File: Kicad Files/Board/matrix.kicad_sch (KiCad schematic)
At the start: 145 parts

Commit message: PCB Space
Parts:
- removed D61, D62, D65, D66, D67, D68: D_Small, symbol mechanical_keyboard:D_Small
- removed MX15, MX47, MX49, MX50, MX51, MX53, MX54, MX55, MX59, MX60, MX61, MX64, MX65, MX66, MX67: MX_SW_solder, PCM_marbastlib-mx:SW_MX_1u, symbol mechanical_keyboard:MX_SW_solder
- removed S1, S2, S3, S4, S5: MX_stab, PCM_marbastlib-mx:STAB_MX_P_6.25u, symbol mechanical_keyboard:MX_stab
- added D1, D74: D_Small, mechanical_keyboard:D_0402_1005Metric, symbol mechanical_keyboard:D_Small
- added MX25: O, mechanical_keyboard:SW_MX_1u, symbol mechanical_keyboard:MX_SW_solder
- added MX26: P, mechanical_keyboard:SW_MX_1u, symbol mechanical_keyboard:MX_SW_solder
- added MX27: [, mechanical_keyboard:SW_MX_1u, symbol mechanical_keyboard:MX_SW_solder
- added MX28: ], mechanical_keyboard:SW_MX_1u, symbol mechanical_keyboard:MX_SW_solder
- added MX29: Enter, mechanical_keyboard:SW_MX_1u, symbol mechanical_keyboard:MX_SW_solder
- added MX30: Insert, mechanical_keyboard:SW_MX_1u, symbol mechanical_keyboard:MX_SW_solder
- added MX42: ', mechanical_keyboard:SW_MX_1u, symbol mechanical_keyboard:MX_SW_solder
- added MX43: \, mechanical_keyboard:SW_MX_1u, symbol mechanical_keyboard:MX_SW_solder
- added MX44: Delete, mechanical_keyboard:SW_MX_1u, symbol mechanical_keyboard:MX_SW_solder
- added MX45: Mode, mechanical_keyboard:SW_MX_1u, symbol mechanical_keyboard:MX_SW_solder
- added MX62: Space, mechanical_keyboard:SW_MX_1u, symbol mechanical_keyboard:MX_SW_solder
- D10, D11, D12, D13, D14, D15, D16, D17, D18, D19, D2, D20, D21, D22, D23, D24, D25, D26, D27, D28, D29, D3, D30, D31, D32, D33, D34, D35, D36, D37, D38, D39, D4, D40, D41, D42, D43, D44, D45, D46, D47, D48, D49, D5, D50, D51, D52, D53, D54, D55, D56, D57, D58, D59, D6, D60, D63, D64, D69, D7, D70, D71, D8, D9: footprint (none) -> mechanical_keyboard:D_0402_1005Metric
- MX1: value MX_SW_solder -> ESC; footprint PCM_marbastlib-mx:SW_MX_1u -> mechanical_keyboard:SW_MX_1u
- MX10: value MX_SW_solder -> 8; footprint PCM_marbastlib-mx:SW_MX_1u -> mechanical_keyboard:SW_MX_1u
- MX11: value MX_SW_solder -> 9; footprint PCM_marbastlib-mx:SW_MX_1u -> mechanical_keyboard:SW_MX_1u
- MX12: value MX_SW_solder -> 0; footprint PCM_marbastlib-mx:SW_MX_1u -> mechanical_keyboard:SW_MX_1u
- MX13: value MX_SW_solder -> -; footprint PCM_marbastlib-mx:SW_MX_1u -> mechanical_keyboard:SW_MX_1u
- MX14: value MX_SW_solder -> +; footprint PCM_marbastlib-mx:SW_MX_1u -> mechanical_keyboard:SW_MX_1u
- MX15: renamed from MX52; value MX_SW_solder -> BackSpace; footprint PCM_marbastlib-mx:SW_MX_1u -> mechanical_keyboard:SW_MX_1u
- MX16: value MX_SW_solder -> Tab; footprint PCM_marbastlib-mx:SW_MX_1u -> mechanical_keyboard:SW_MX_1u
- MX17: value MX_SW_solder -> Q; footprint PCM_marbastlib-mx:SW_MX_1u -> mechanical_keyboard:SW_MX_1u
- MX18: value MX_SW_solder -> W; footprint PCM_marbastlib-mx:SW_MX_1u -> mechanical_keyboard:SW_MX_1u
- MX19: value MX_SW_solder -> E; footprint PCM_marbastlib-mx:SW_MX_1u -> mechanical_keyboard:SW_MX_1u
- MX2: value MX_SW_solder -> `; footprint PCM_marbastlib-mx:SW_MX_1u -> mechanical_keyboard:SW_MX_1u
- MX20: value MX_SW_solder -> R; footprint PCM_marbastlib-mx:SW_MX_1u -> mechanical_keyboard:SW_MX_1u
- MX21: value MX_SW_solder -> T; footprint PCM_marbastlib-mx:SW_MX_1u -> mechanical_keyboard:SW_MX_1u
- MX22: value MX_SW_solder -> Y; footprint PCM_marbastlib-mx:SW_MX_1u -> mechanical_keyboard:SW_MX_1u
- MX23: value MX_SW_solder -> U; footprint PCM_marbastlib-mx:SW_MX_1u -> mechanical_keyboard:SW_MX_1u
- MX24: value MX_SW_solder -> I; footprint PCM_marbastlib-mx:SW_MX_1u -> mechanical_keyboard:SW_MX_1u
- MX3: value MX_SW_solder -> 1; footprint PCM_marbastlib-mx:SW_MX_1u -> mechanical_keyboard:SW_MX_1u
- MX31: renamed from MX25; value MX_SW_solder -> CapsLock; footprint PCM_marbastlib-mx:SW_MX_1u -> mechanical_keyboard:SW_MX_1u
- MX32: renamed from MX27; value MX_SW_solder -> A; footprint PCM_marbastlib-mx:SW_MX_1u -> mechanical_keyboard:SW_MX_1u
- MX33: renamed from MX29; value MX_SW_solder -> S; footprint PCM_marbastlib-mx:SW_MX_1u -> mechanical_keyboard:SW_MX_1u
- MX34: renamed from MX31; value MX_SW_solder -> D; footprint PCM_marbastlib-mx:SW_MX_1u -> mechanical_keyboard:SW_MX_1u
- MX35: renamed from MX33; value MX_SW_solder -> F; footprint PCM_marbastlib-mx:SW_MX_1u -> mechanical_keyboard:SW_MX_1u
- MX36: renamed from MX35; value MX_SW_solder -> G; footprint PCM_marbastlib-mx:SW_MX_1u -> mechanical_keyboard:SW_MX_1u
- MX37: value MX_SW_solder -> H; footprint PCM_marbastlib-mx:SW_MX_1u -> mechanical_keyboard:SW_MX_1u
- MX38: renamed from MX39; value MX_SW_solder -> J; footprint PCM_marbastlib-mx:SW_MX_1u -> mechanical_keyboard:SW_MX_1u
- MX39: renamed from MX41; value MX_SW_solder -> K; footprint PCM_marbastlib-mx:SW_MX_1u -> mechanical_keyboard:SW_MX_1u
- MX4: value MX_SW_solder -> 2; footprint PCM_marbastlib-mx:SW_MX_1u -> mechanical_keyboard:SW_MX_1u
- MX40: renamed from MX43; value MX_SW_solder -> L; footprint PCM_marbastlib-mx:SW_MX_1u -> mechanical_keyboard:SW_MX_1u
- MX41: renamed from MX45; value MX_SW_solder -> ;; footprint PCM_marbastlib-mx:SW_MX_1u -> mechanical_keyboard:SW_MX_1u
- MX46: renamed from MX26; value MX_SW_solder -> LShift; footprint PCM_marbastlib-mx:SW_MX_1u -> mechanical_keyboard:SW_MX_1u
- MX47: renamed from MX28; value MX_SW_solder -> Z; footprint PCM_marbastlib-mx:SW_MX_1u -> mechanical_keyboard:SW_MX_1u
- MX48: renamed from MX30; value MX_SW_solder -> X; footprint PCM_marbastlib-mx:SW_MX_1u -> mechanical_keyboard:SW_MX_1u
- MX49: renamed from MX32; value MX_SW_solder -> C; footprint PCM_marbastlib-mx:SW_MX_1u -> mechanical_keyboard:SW_MX_1u
- MX5: value MX_SW_solder -> 3; footprint PCM_marbastlib-mx:SW_MX_1u -> mechanical_keyboard:SW_MX_1u
- MX50: renamed from MX34; value MX_SW_solder -> V; footprint PCM_marbastlib-mx:SW_MX_1u -> mechanical_keyboard:SW_MX_1u
- MX51: renamed from MX36; value MX_SW_solder -> B; footprint PCM_marbastlib-mx:SW_MX_1u -> mechanical_keyboard:SW_MX_1u
- MX52: renamed from MX38; value MX_SW_solder -> N; footprint PCM_marbastlib-mx:SW_MX_1u -> mechanical_keyboard:SW_MX_1u
- MX53: renamed from MX40; value MX_SW_solder -> M; footprint PCM_marbastlib-mx:SW_MX_1u -> mechanical_keyboard:SW_MX_1u
- MX54: renamed from MX42; value MX_SW_solder -> ,; footprint PCM_marbastlib-mx:SW_MX_1u -> mechanical_keyboard:SW_MX_1u
- MX55: renamed from MX44; value MX_SW_solder -> .; footprint PCM_marbastlib-mx:SW_MX_1u -> mechanical_keyboard:SW_MX_1u
- MX56: renamed from MX46; value MX_SW_solder -> /; footprint PCM_marbastlib-mx:SW_MX_1u -> mechanical_keyboard:SW_MX_1u
- MX57: renamed from MX48; value MX_SW_solder -> RShift; footprint PCM_marbastlib-mx:SW_MX_1u -> mechanical_keyboard:SW_MX_1u
- MX58: renamed from MX70; value MX_SW_solder -> Up; footprint PCM_marbastlib-mx:SW_MX_1u -> mechanical_keyboard:SW_MX_1u
- MX59: renamed from MX56; value MX_SW_solder -> LCtrl; footprint PCM_marbastlib-mx:SW_MX_1u -> mechanical_keyboard:SW_MX_1u
- MX6: value MX_SW_solder -> 4; footprint PCM_marbastlib-mx:SW_MX_1u -> mechanical_keyboard:SW_MX_1u
- MX60: renamed from MX57; value MX_SW_solder -> Windows; footprint PCM_marbastlib-mx:SW_MX_1u -> mechanical_keyboard:SW_MX_1u
- MX61: renamed from MX58; value MX_SW_solder -> LAlt; footprint PCM_marbastlib-mx:SW_MX_1u -> mechanical_keyboard:SW_MX_1u
- MX63: value MX_SW_solder -> FN; footprint PCM_marbastlib-mx:SW_MX_1u -> mechanical_keyboard:SW_MX_1u
- MX64: renamed from MX62; value MX_SW_solder -> Left; footprint PCM_marbastlib-mx:SW_MX_1u -> mechanical_keyboard:SW_MX_1u
- MX65: renamed from MX68; value MX_SW_solder -> Down; footprint PCM_marbastlib-mx:SW_MX_1u -> mechanical_keyboard:SW_MX_1u
- MX66: renamed from MX69; value MX_SW_solder -> Right; footprint PCM_marbastlib-mx:SW_MX_1u -> mechanical_keyboard:SW_MX_1u
- MX7: value MX_SW_solder -> 5; footprint PCM_marbastlib-mx:SW_MX_1u -> mechanical_keyboard:SW_MX_1u
- MX8: value MX_SW_solder -> 6; footprint PCM_marbastlib-mx:SW_MX_1u -> mechanical_keyboard:SW_MX_1u
- MX9: value MX_SW_solder -> 7; footprint PCM_marbastlib-mx:SW_MX_1u -> mechanical_keyboard:SW_MX_1u
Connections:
- net COL14 is gone; now on net COL12: MX58.1, MX65.1
- net COL15 is gone; now on net COL13: MX66.1
- net COL0: now also MX1.1, MX16.1, MX31.1, MX46.1, MX59.1
- net COL1: now also MX17.1, MX2.1, MX32.1, MX47.1, MX60.1; no longer MX1.1, MX13.1, MX31.1, MX46.1, MX59.1
- net COL10: now also MX11.1, MX41.1, MX56.1, MX26.1; no longer MX10.1, MX22.1, MX40.1, MX55.1
- net COL11: now also MX12.1, MX57.1, MX64.1, MX27.1, MX42.1; no longer MX11.1, MX23.1, MX41.1, MX56.1
- net COL12: now also MX13.1, MX28.1, MX43.1; no longer MX12.1, MX24.1, MX57.1
- net COL13: now also MX14.1, MX29.1, MX30.1, MX44.1, MX45.1; no longer MX64.1
- net COL2: now also MX18.1, MX3.1, MX33.1, MX48.1, MX61.1; no longer MX14.1, MX2.1, MX32.1, MX47.1, MX60.1
- net COL3: now also MX19.1, MX34.1, MX4.1, MX49.1, MX62.1; no longer MX3.1, MX33.1, MX48.1, MX61.1
- net COL4: now also MX20.1, MX35.1, MX5.1, MX50.1; no longer MX16.1, MX34.1, MX4.1, MX49.1
- net COL5: now also MX21.1, MX36.1, MX51.1, MX6.1; no longer MX17.1, MX35.1, MX5.1, MX50.1
- net COL6: now also MX22.1, MX37.1, MX52.1, MX7.1; no longer MX18.1, MX36.1, MX51.1, MX6.1
- net COL7: now also MX23.1, MX38.1, MX53.1, MX63.1, MX8.1; no longer MX19.1, MX37.1, MX52.1, MX7.1
- net COL8: now also MX24.1, MX39.1, MX54.1, MX9.1; no longer MX20.1, MX38.1, MX53.1, MX63.1, MX8.1
- net COL9: now also MX10.1, MX40.1, MX55.1, MX25.1; no longer MX21.1, MX39.1, MX54.1, MX9.1
- net ROW0: now also D1.1 (K), D74.1 (K); no longer D48.1 (K), D54.1 (K), D55.1 (K)
- net ROW1: now also D48.1 (K), D55.1 (K); no longer D60.1 (K)
- net ROW2: now also D52.1 (K), D56.1 (K), D60.1 (K)
- net ROW3: no longer D52.1 (K)
- net ROW4: now also D54.1 (K); no longer D56.1 (K)
- net at D17.2 (A): now also MX19.2; no longer MX16.2
- net at D25.2 (A): now also MX27.2; no longer MX24.2
- net at D16.2 (A): now also MX18.2
- net at D18.2 (A): now also MX20.2; no longer MX17.2
- net at MX14.2: now also D74.2 (A); no longer D15.2 (A)
- net at D51.2 (A): now also MX42.2
- net at MX23.2: now also D21.2 (A); no longer D24.2 (A)
- net at D50.2 (A): now also MX29.2
- net at D20.2 (A): now also MX22.2; no longer MX19.2
- net at D54.2 (A): now also MX62.2
- net at D60.2 (A): now also MX45.2
- net at D23.2 (A): now also MX25.2; no longer MX22.2
- net at MX21.2: now also D19.2 (A); no longer D22.2 (A)
- net at D56.2 (A): now also MX44.2
- net at D55.2 (A): now also MX30.2
- net at D14.2 (A): now also MX16.2; no longer MX13.2
- net at D52.2 (A): now also MX43.2
- net EC1_SW1: no longer names the net of D48.2 (A)
- net EC1_SW1: now also MX28.2
- new net: D24.2 (A), MX26.2
- new net: D22.2 (A), MX24.2
- new net: D1.2 (A), MX13.2
- new net: D15.2 (A), MX17.2
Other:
- moved on the sheet: D10, D11, D12, D13, D14, D15, D16, D17, D18, D19, D2, D20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

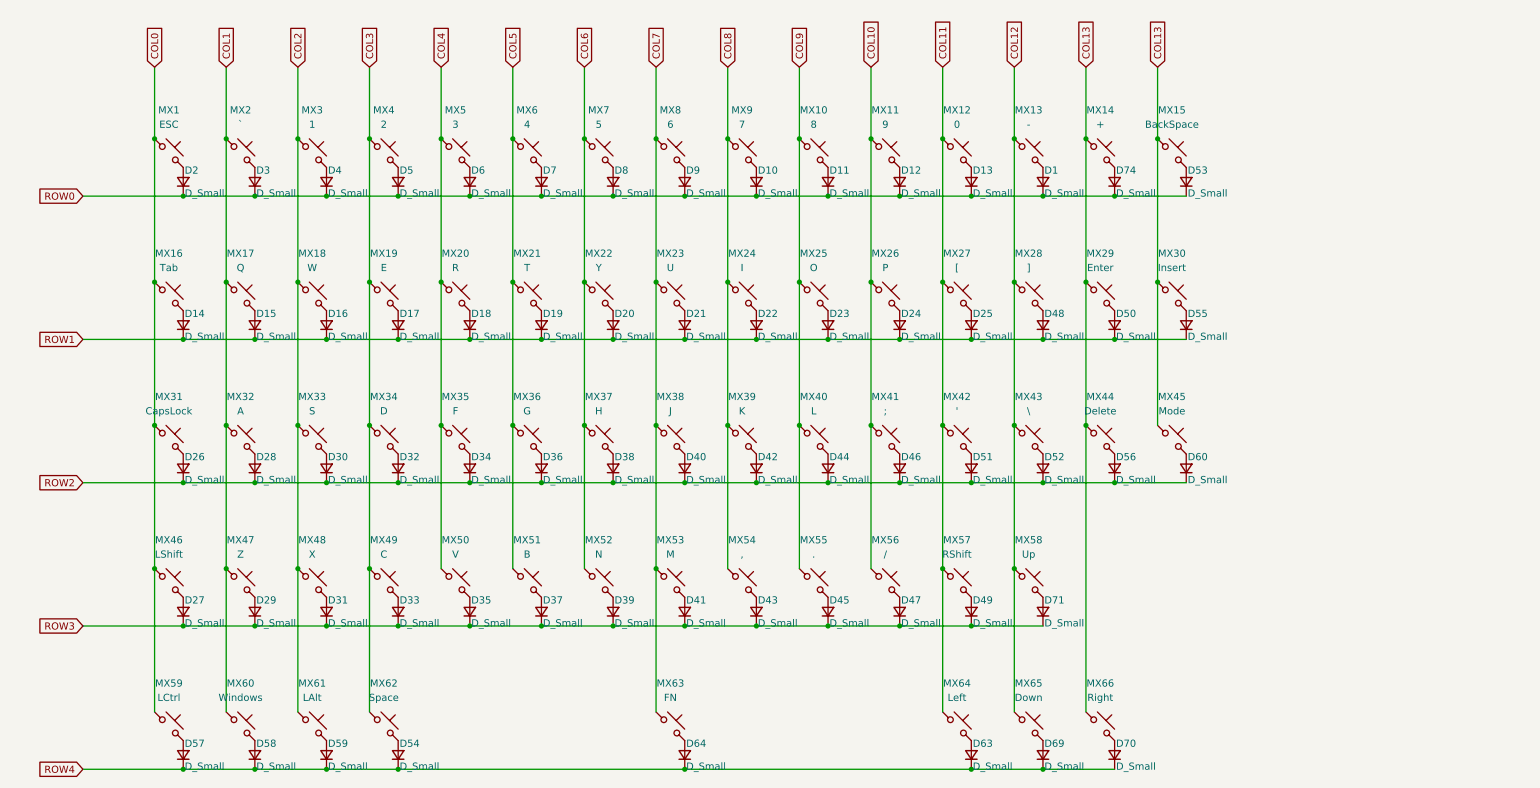
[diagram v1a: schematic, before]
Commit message: Matrix and Diode Done
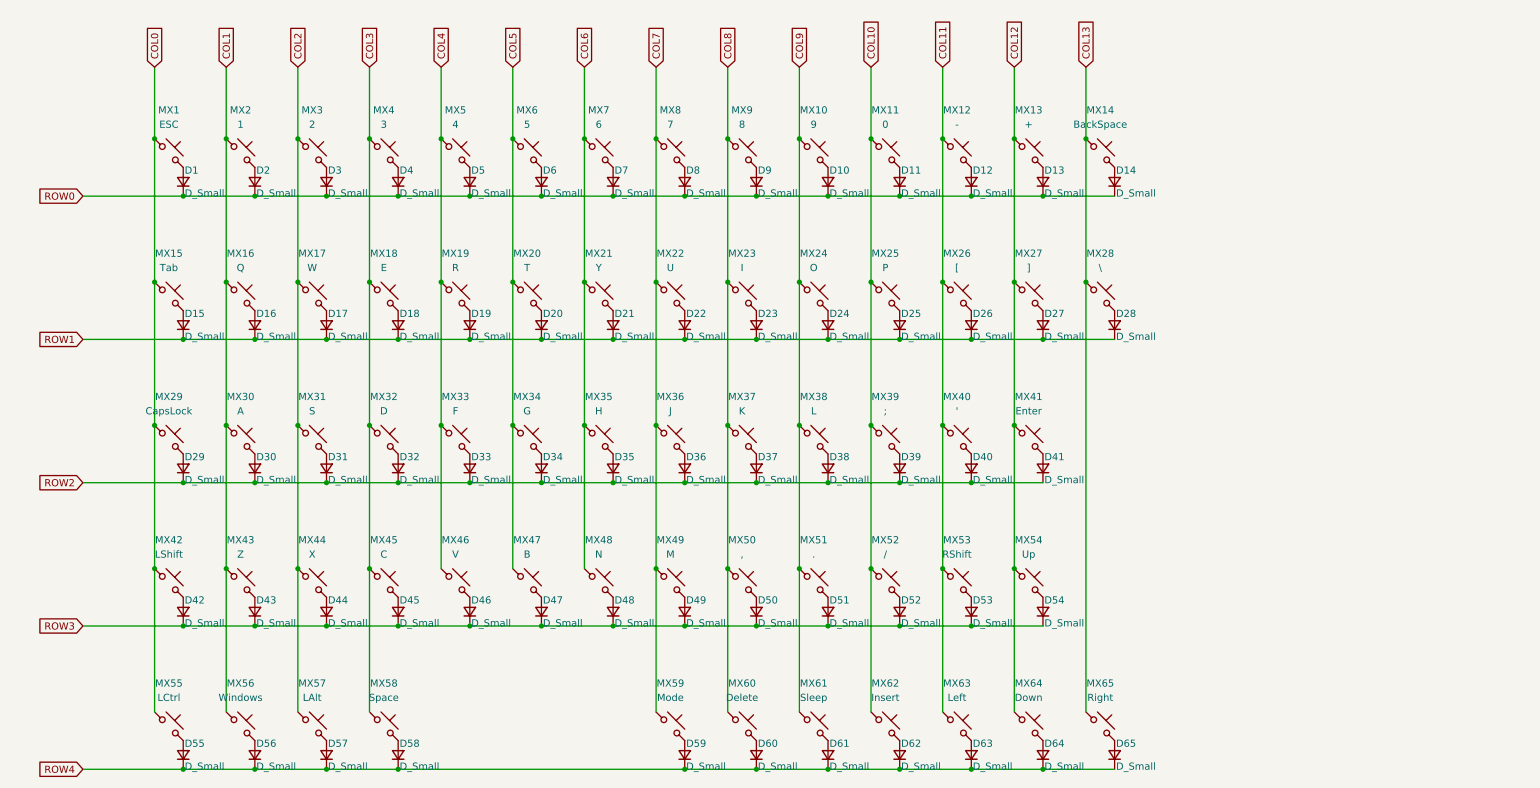
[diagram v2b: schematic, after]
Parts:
- removed D1, D55, D56, D71, D74: D_Small, mechanical_keyboard:D_0402_1005Metric, symbol mechanical_keyboard:D_Small
- removed MX55: ., mechanical_keyboard:SW_MX_1u, symbol mechanical_keyboard:MX_SW_solder
- removed MX56: /, mechanical_keyboard:SW_MX_1u, symbol mechanical_keyboard:MX_SW_solder
- removed MX57: RShift, mechanical_keyboard:SW_MX_1u, symbol mechanical_keyboard:MX_SW_solder
- removed MX58: Up, mechanical_keyboard:SW_MX_1u, symbol mechanical_keyboard:MX_SW_solder
- added D2, D54, D61, D62: D_Small, mechanical_keyboard:D_0402_1005Metric, symbol mechanical_keyboard:D_Small
- added MX60: Delete, mechanical_keyboard:SW_MX_1u, symbol mechanical_keyboard:MX_SW_solder
- added MX61: Sleep, mechanical_keyboard:SW_MX_1u, symbol mechanical_keyboard:MX_SW_solder
- added MX62: Insert, mechanical_keyboard:SW_MX_1u, symbol mechanical_keyboard:MX_SW_solder
- MX10: value 8 -> 9
- MX11: value 9 -> 0
- MX12: value 0 -> -
- MX13: value - -> +
- MX14: value + -> BackSpace
- MX15: value BackSpace -> Tab
- MX16: value Tab -> Q
- MX17: value Q -> W
- MX18: value W -> E
- MX19: value E -> R
- MX2: value ` -> 1
- MX20: value R -> T
- MX21: value T -> Y
- MX22: value Y -> U
- MX23: value U -> I
- MX24: value I -> O
- MX25: value O -> P
- MX26: value P -> [
- MX27: value [ -> ]
- MX28: value ] -> \
- MX29: value Enter -> CapsLock
- MX3: value 1 -> 2
- MX30: value Insert -> A
- MX31: value CapsLock -> S
- MX32: value A -> D
- MX33: value S -> F
- MX34: value D -> G
- MX35: value F -> H
- MX36: value G -> J
- MX37: value H -> K
- MX38: value J -> L
- MX39: value K -> ;
- MX4: value 2 -> 3
- MX40: value L -> '
- MX41: value ; -> Enter
- MX42: value ' -> LShift
- MX43: value \ -> Z
- MX44: value Delete -> X
- MX45: value Mode -> C
- MX46: value LShift -> V
- MX47: value Z -> B
- MX48: value X -> N
- MX49: value C -> M
- MX5: value 3 -> 4
- MX50: value V -> ,
- MX51: value B -> .
- MX52: value N -> /
- MX53: value M -> RShift
- MX54: value , -> Up
- MX59: renamed from MX63; value FN -> Mode
- MX6: value 4 -> 5
- MX7: value 5 -> 6
- MX8: value 6 -> 7
- MX9: value 7 -> 8
- renumbered D2 to D1, D57 to D55, D58 to D56, D59 to D57, D54 to D58, D64 to D59, D69 to D64, D70 to D65, MX59 to MX55, MX60 to MX56, MX61 to MX57, MX62 to MX58, MX64 to MX63, MX65 to MX64, MX66 to MX65
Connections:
- net COL0: now also MX15.1, MX29.1, MX42.1; no longer MX16.1, MX31.1, MX46.1
- net COL1: now also MX16.1, MX30.1, MX43.1; no longer MX17.1, MX32.1, MX47.1
- net COL10: now also MX25.1, MX39.1, MX52.1, MX62.1; no longer MX26.1, MX41.1
- net COL11: now also MX26.1, MX40.1, MX53.1; no longer MX27.1, MX42.1
- net COL12: now also MX27.1, MX41.1, MX54.1; no longer MX28.1, MX43.1
- net COL13: now also MX28.1; no longer MX15.1, MX29.1, MX30.1, MX44.1, MX45.1
- net COL2: now also MX17.1, MX31.1, MX44.1; no longer MX18.1, MX33.1, MX48.1
- net COL3: now also MX18.1, MX32.1, MX45.1; no longer MX19.1, MX34.1, MX49.1
- net COL4: now also MX19.1, MX33.1, MX46.1; no longer MX20.1, MX35.1, MX50.1
- net COL5: now also MX20.1, MX34.1, MX47.1; no longer MX21.1, MX36.1, MX51.1
- net COL6: now also MX21.1, MX35.1, MX48.1; no longer MX22.1, MX37.1, MX52.1
- net COL7: now also MX22.1, MX36.1, MX49.1; no longer MX23.1, MX38.1, MX53.1
- net COL8: now also MX23.1, MX37.1, MX50.1, MX60.1; no longer MX24.1, MX39.1, MX54.1
- net COL9: now also MX24.1, MX38.1, MX51.1, MX61.1; no longer MX25.1, MX40.1
- net ROW0: now also D14.1 (K), D2.1 (K); no longer D53.1 (K)
- net ROW1: now also D26.1 (K), D27.1 (K), D28.1 (K); no longer D14.1 (K), D48.1 (K), D50.1 (K)
- net ROW2: now also D29.1 (K), D31.1 (K), D33.1 (K), D35.1 (K), D37.1 (K), D39.1 (K), D41.1 (K); no longer D26.1 (K), D28.1 (K), D42.1 (K), D44.1 (K), D46.1 (K), D51.1 (K), D52.1 (K), D60.1 (K)
- net ROW3: now also D42.1 (K), D44.1 (K), D46.1 (K), D48.1 (K), D50.1 (K), D51.1 (K), D52.1 (K), D53.1 (K), D54.1 (K); no longer D27.1 (K), D29.1 (K), D31.1 (K), D33.1 (K), D35.1 (K), D37.1 (K), D39.1 (K), D41.1 (K)
- net ROW4: now also D60.1 (K), D61.1 (K), D62.1 (K)
- net at MX45.2: now also D45.2 (A); no longer D60.2 (A)
- net at MX40.2: now also D40.2 (A); no longer D44.2 (A)
- net at MX39.2: now also D39.2 (A); no longer D42.2 (A)
- net at D51.2 (A): now also MX51.2; no longer MX42.2
- net at MX21.2: now also D21.2 (A); no longer D19.2 (A)
- net at D17.2 (A): now also MX17.2; no longer MX19.2
- net at D11.2 (A): now also MX11.2; no longer MX10.2
- net at MX15.2: now also D15.2 (A); no longer D53.2 (A)
- net at MX14.2: now also D14.2 (A)
- net at D28.2 (A): now also MX28.2; no longer MX32.2
- net at MX48.2: now also D48.2 (A); no longer D31.2 (A)
- net at MX5.2: now also D5.2 (A); no longer D6.2 (A)
- net at MX22.2: now also D22.2 (A); no longer D20.2 (A)
- net at D25.2 (A): now also MX25.2; no longer MX27.2
- net at MX46.2: now also D46.2 (A); no longer D27.2 (A)
- net at D35.2 (A): now also MX35.2; no longer MX50.2
- net at MX18.2: now also D18.2 (A); no longer D16.2 (A)
- net at D7.2 (A): now also MX7.2; no longer MX6.2
- net at D29.2 (A): now also MX29.2; no longer MX47.2
- net at MX20.2: now also D20.2 (A); no longer D18.2 (A)
- net at MX23.2: now also D23.2 (A); no longer D21.2 (A)
- net at D4.2 (A): now also MX4.2; no longer MX3.2
- net at D12.2 (A): now also MX12.2; no longer MX11.2
- net at D38.2 (A): now also MX38.2; no longer MX37.2
- net at MX31.2: now also D31.2 (A); no longer D26.2 (A)
- net at D37.2 (A): now also MX37.2; no longer MX51.2
- net at MX26.2: now also D26.2 (A); no longer D24.2 (A)
- net at MX34.2: now also D34.2 (A); no longer D32.2 (A)
- net at MX24.2: now also D24.2 (A); no longer D22.2 (A)
- net at MX44.2: now also D44.2 (A)
- net at MX9.2: now also D9.2 (A); no longer D10.2 (A)
- net at MX41.2: now also D41.2 (A); no longer D46.2 (A)
- net at MX49.2: now also D49.2 (A); no longer D33.2 (A)
- net at MX2.2: now also D2.2 (A); no longer D3.2 (A)
- net at MX52.2: now also D52.2 (A); no longer D39.2 (A)
- net at D8.2 (A): now also MX8.2; no longer MX7.2
- net at D13.2 (A): now also MX13.2; no longer MX12.2
- net at MX54.2: now also D54.2 (A); no longer D43.2 (A)
- net at MX43.2: now also D43.2 (A); no longer D52.2 (A)
- net at D50.2 (A): now also MX50.2; no longer MX29.2
- net at MX16.2: now also D16.2 (A); no longer D14.2 (A)
- net at MX30.2: now also D30.2 (A)
- net at MX33.2: now also D33.2 (A); no longer D30.2 (A)
- net at MX53.2: now also D53.2 (A); no longer D41.2 (A)
- net at D47.2 (A): now also MX47.2
- new net: D61.2 (A), MX61.2
- new net: D32.2 (A), MX32.2
- new net: D6.2 (A), MX6.2
- new net: D62.2 (A), MX62.2
- new net: D27.2 (A), MX27.2
- new net: D60.2 (A), MX60.2
- new net: D3.2 (A), MX3.2
- new net: D10.2 (A), MX10.2
- new net: D42.2 (A), MX42.2
- new net: D19.2 (A), MX19.2

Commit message: Switch Update
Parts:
- added D66: D_Small, mechanical_keyboard:D_0402_1005Metric, symbol mechanical_keyboard:D_Small
- added MX66: Delete, mechanical_keyboard:SW_Cherry_MX_1.00u_PCB, symbol mechanical_keyboard:MX_SW_solder
- MX1, MX10, MX11, MX12, MX13, MX14, MX15, MX16, MX17, MX18, MX19, MX2, MX20, MX21, MX22, MX23, MX24, MX25, MX26, MX27, MX28, MX29, MX3, MX30, MX31, MX32, MX33, MX34, MX35, MX36, MX37, MX38, MX39, MX4, MX40, MX41, MX42, MX43, MX44, MX45, MX46, MX47, MX48, MX49, MX5, MX50, MX51, MX52, MX53, MX54, MX55, MX56, MX57, MX58, MX6, MX62, MX63, MX64, MX65, MX7, MX8, MX9: footprint mechanical_keyboard:SW_MX_1u -> mechanical_keyboard:SW_Cherry_MX_1.00u_PCB
- MX59: value Mode -> RAlt; footprint mechanical_keyboard:SW_MX_1u -> mechanical_keyboard:SW_Cherry_MX_1.00u_PCB
- MX60: value Delete -> Mode; footprint mechanical_keyboard:SW_MX_1u -> mechanical_keyboard:SW_Cherry_MX_1.00u_PCB
- MX61: value Sleep -> LCtrl; footprint mechanical_keyboard:SW_MX_1u -> mechanical_keyboard:SW_Cherry_MX_1.00u_PCB
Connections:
- net COL10: now also MX63.1; no longer MX62.1
- net COL11: now also MX64.1; no longer MX63.1
- net COL12: now also MX65.1; no longer MX64.1
- net COL13: now also MX62.1, MX66.1; no longer MX65.1
- net ROW2: now also D62.1 (K)
- net ROW3: now also D66.1 (K)
- net ROW4: no longer D62.1 (K)
- new net: D66.2 (A), MX66.2

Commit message: Routing Completed
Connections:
- net COL10: now also MX61.1; no longer MX63.1
- net COL11: now also MX63.1; no longer MX64.1
- net COL12: no longer MX54.1, MX65.1
- net COL13: now also MX54.1, MX64.1; no longer MX62.1, MX66.1
- net COL3: no longer MX58.1
- net COL5: now also MX58.1
- net COL7: no longer MX59.1
- net COL8: now also MX59.1; no longer MX60.1
- net COL9: now also MX60.1; no longer MX61.1
- net ROW0: now also D62.1 (K)
- net ROW1: now also D66.1 (K)
- net ROW2: no longer D62.1 (K)
- net ROW3: no longer D66.1 (K)
- new net COL14: MX62.1, MX65.1, MX66.1
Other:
- moved on the sheet: D54, D58, D59, D60, D61, D62, D63, D64, D65, D66, MX54, MX58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
